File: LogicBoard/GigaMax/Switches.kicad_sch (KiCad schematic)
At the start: 32 parts, among them U17 RS2057XH, U18 RS2057XH, U19 RS2057XH, U20 RS2057XH, U21 RS2057XH, U22 RS2057XH, U5 RS2057XH

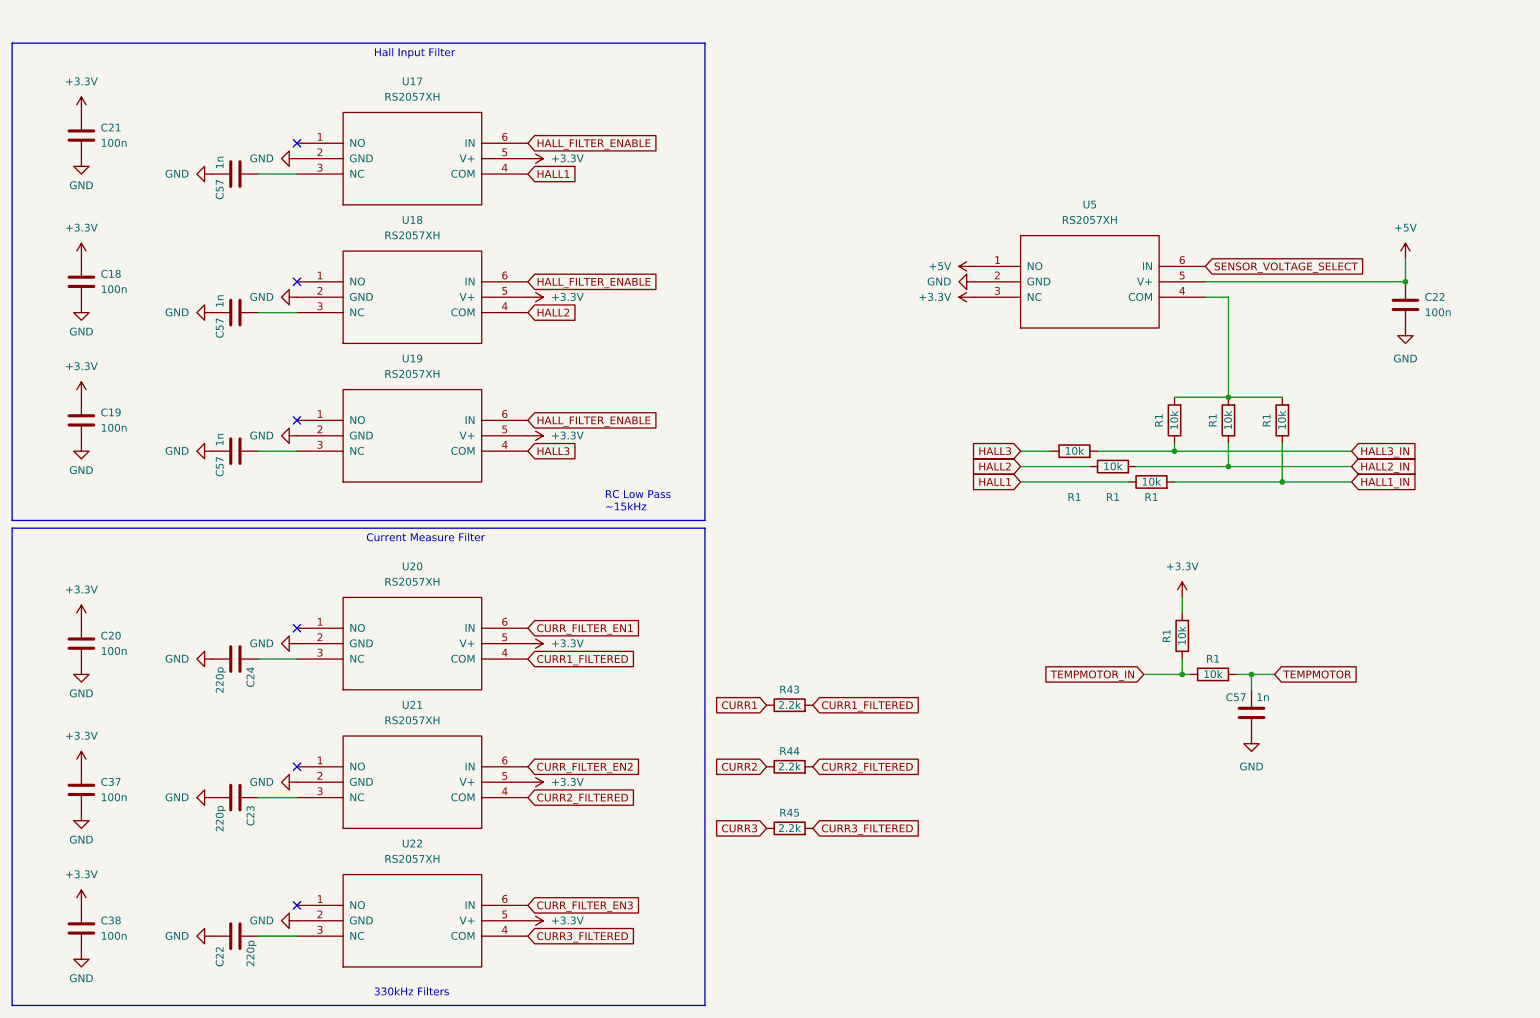
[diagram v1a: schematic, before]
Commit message: v2.8.0 - Small Hall sensors
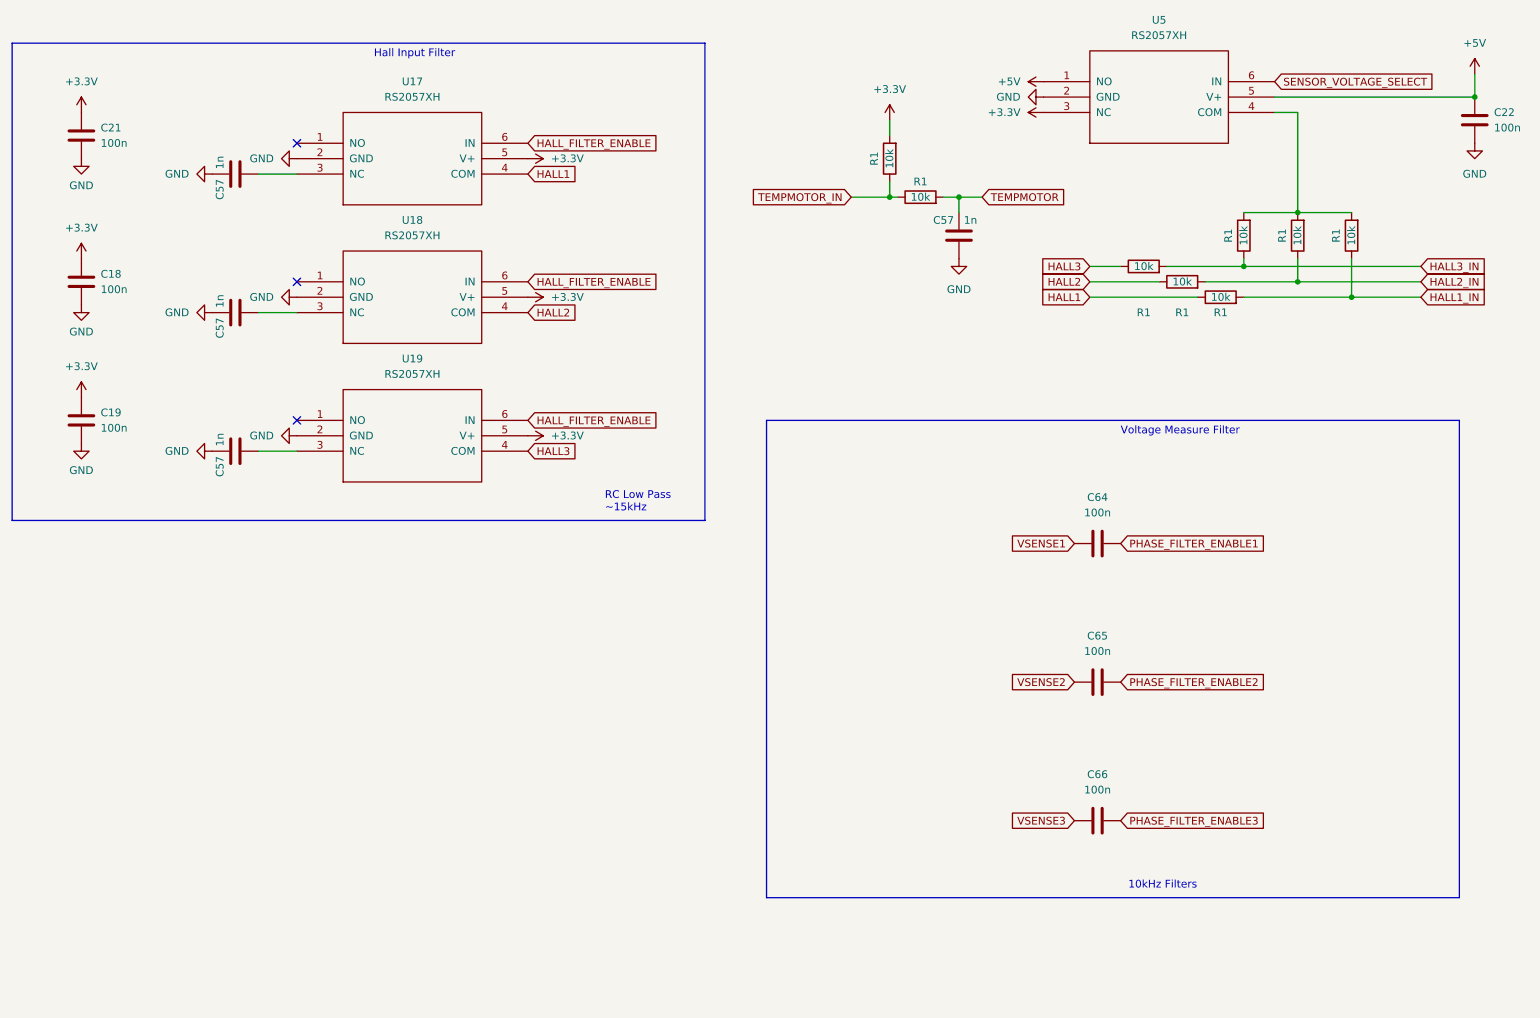
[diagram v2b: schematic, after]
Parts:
- removed C20, C37, C38: 100n, GigaVescLibs:C_0603_1608Metric_L, symbol Device:C
- removed C22, C23, C24: 220p, GigaVescLibs:C_0603_1608Metric_L, symbol Device:C
- removed R43, R44, R45: 2.2k, Resistor_SMD:R_0603_1608Metric, symbol Device:R
- removed U20, U21, U22: RS2057XH, Package_TO_SOT_SMD:SOT-23-6, symbol GigaVescSymbols:RS2057XH
- added C64, C65, C66: 100n, GigaVescLibs:C_0603_1608Metric_L, symbol Device:C
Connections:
- new net PHASE_FILTER_ENABLE1: C64.2
- new net PHASE_FILTER_ENABLE2: C65.2
- new net PHASE_FILTER_ENABLE3: C66.2
- new net VSENSE1: C64.1
- new net VSENSE2: C65.1
- new net VSENSE3: C66.1
- no-connect marks 6 -> 3
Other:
- note added: "10kHz Filters"
- note added: "Voltage Measure Filter"
- note removed: "330kHz Filters"
- note removed: "Current Measure Filter"
- moved on the sheet: C22, C57, R1, U5
